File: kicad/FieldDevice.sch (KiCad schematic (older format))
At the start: 13 parts

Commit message: Adding more features to the design
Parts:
- removed RV?: POT, symbol POT
- added J? (x4): JUMPER_1x2, symbol JUMPER_1x2
- added R? (x4): NPOP, symbol R
- added SW? (x2): SW_PUSH, symbol SW_PUSH
- added U?: MCP4017T-502E, symbol MCP4017T-502E
- R?: value 0 -> 0Ω
- R?: value 10k -> 9k1Ω
- R?: value 5k -> 4k7Ω
- TH?: value THERMISTOR -> PTC
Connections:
- net labels added: Display, OverTemp, Set
- wire segments 44 -> 73
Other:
- note added: "# Seperate ADC for isolation away from the Micro. \n Would this be advixable/necessary?\n# Would the PTC really provide any form of protection?\n# Could a Digital Potentiometer be used here?\n# How would this really be calibrated?\n"
- note added: "Hard wired I²C \naddress '0101111'"
- note added: "I²C Address '1010000'"
- note added: "The minimal configuration for the XBEE is \nVcc, GND, DIN and DOUT"
- moved on the sheet: D?, H?, R?, TH?

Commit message: Completed schematic, layout and gerbers. 2L_1
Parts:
- removed D?: D, symbol D
- removed J? (x4): JUMPER_1x2, symbol JUMPER_1x2
- removed R?: 9k1Ω, symbol R
- removed R?: 4k7Ω, symbol R
- removed R? (x4): NPOP, symbol R
- removed SW? (x2): SW_PUSH, symbol SW_PUSH
- removed TH?: PTC, symbol THERMISTOR
- removed U?: MCP4017T-502E, symbol MCP4017T-502E
- added R102, R107, R108: 0Ω, Resistors_SMD:R_0805, symbol R
- added R103, R110: 4k7Ω, Resistors_SMD:R_0805, symbol R
- H101: renamed from H?; footprint (none) -> CE_Header:CE_Header
- H102: renamed from H?; footprint (none) -> FieldDevice_Footprints:XBEE_S2C
- R101, R104, R105, R106, R109: renamed from R?; footprint (none) -> Resistors_SMD:R_0805
- U101: renamed from U?; footprint (none) -> Housings_SOIC:SOIC-8_3.9x4.9mm_Pitch1.27mm
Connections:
- net labels added: ANLG_1, CLK, CS, MOSI, REG_SEL
- net labels removed: Set, TEST_NEG, TEST_POS, VMesure
- wire segments 73 -> 56
- no-connect marks 14 -> 17
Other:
- note removed: "Fixed address of 0x90"
- note removed: "Hard wired I²C \naddress '0101111'"
- note removed: "Voltage Sensor"

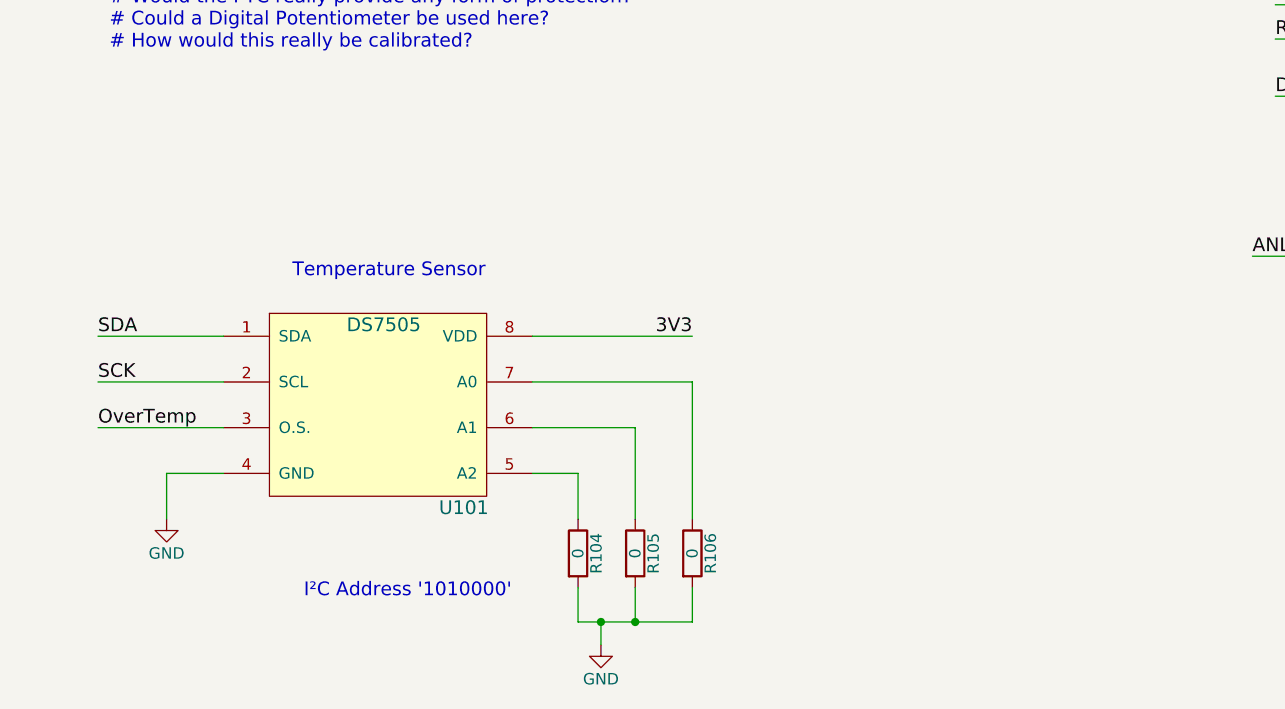
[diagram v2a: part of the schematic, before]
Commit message: added the missing pullup resistors 2L_2
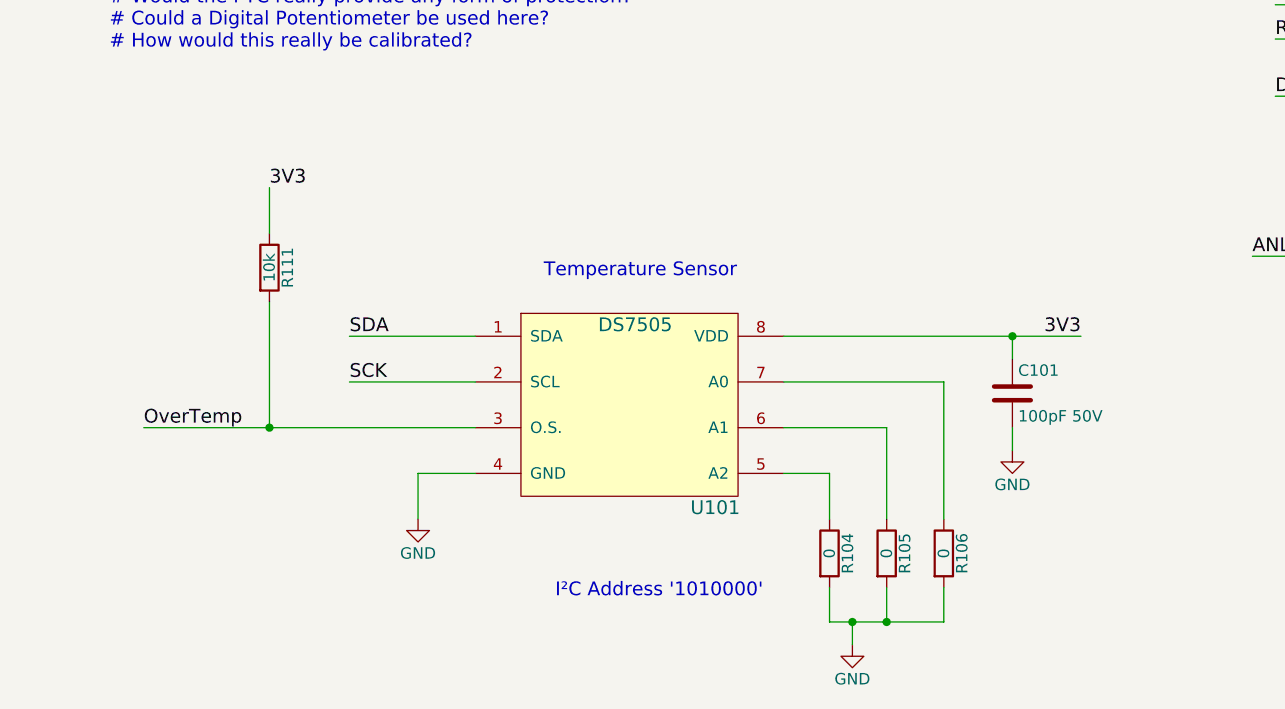
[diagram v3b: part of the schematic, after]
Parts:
- added C101: 100pF 50V, Capacitors_SMD:C_0805, symbol C
- added R111: 10k, Resistors_SMD:R_0805, symbol R
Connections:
- net 3V3: now also C101.1, R111.1
- net GND: now also C101.2
- net OverTemp: now also R111.2
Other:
- moved on the sheet: R104, R105, R106, U101
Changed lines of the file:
@@
 L DS7505 U101
 U 1 1 59347421
-P 2250 6100
-F 0 "U101" H 2600 5650 60  0000 C CNN
-F 1 "DS7505" H 2250 6450 60  0000 C CNN
-F 2 "Housings_SOIC:SOIC-8_3.9x4.9mm_Pitch1.27mm" H 2250 5900 60  0001 C CNN
-F 3 "" H 2250 5900 60  0000 C CNN
-	1    2250 6100
-	1    0    0    -1
-$EndComp
-Text Label 3600 5800 2    60   ~ 0
+P 3350 6100
+F 0 "U101" H 3700 5650 60  0000 C CNN
+F 1 "DS7505" H 3350 6450 60  0000 C CNN
+F 2 "Housings_SOIC:SOIC-8_3.9x4.9mm_Pitch1.27mm" H 3350 5900 60  0001 C CNN
+F 3 "" H 3350 5900 60  0000 C CNN
+	1    3350 6100
+	1    0    0    -1
+$EndComp
+Text Label 5300 5800 2    60   ~ 0
 3V3
 $Comp
 L GND #PWR04
 U 1 1 59347521
-P 1300 6600
-F 0 "#PWR04" H 1300 6350 50  0001 C CNN
-F 1 "GND" H 1300 6450 50  0000 C CNN
-F 2 "" H 1300 6600 50  0000 C CNN
-F 3 "" H 1300 6600 50  0000 C CNN
-	1    1300 6600
+P 2400 6600
+F 0 "#PWR04" H 2400 6350 50  0001 C CNN
+F 1 "GND" H 2400 6450 50  0000 C CNN
+F 2 "" H 2400 6600 50  0000 C CNN
+F 3 "" H 2400 6600 50  0000 C CNN
+	1    2400 6600
 	1    0    0    -1
 $EndComp
@@
 L R R104
 U 1 1 593475EC
-P 3100 6750
-F 0 "R104" V 3180 6750 50  0000 C CNN
-F 1 "0" V 3100 6750 50  0000 C CNN
-F 2 "Resistors_SMD:R_0805" V 3030 6750 50  0001 C CNN
-F 3 "" H 3100 6750 50  0000 C CNN
-	1    3100 6750
+P 4200 6750
+F 0 "R104" V 4280 6750 50  0000 C CNN
+F 1 "0" V 4200 6750 50  0000 C CNN
+F 2 "Resistors_SMD:R_0805" V 4130 6750 50  0001 C CNN
+F 3 "" H 4200 6750 50  0000 C CNN
+	1    4200 6750
 	1    0    0    -1
 $EndComp
@@
 L R R105
 U 1 1 59347631
-P 3350 6750
-F 0 "R105" V 3430 6750 50  0000 C CNN
-F 1 "0" V 3350 6750 50  0000 C CNN
-F 2 "Resistors_SMD:R_0805" V 3280 6750 50  0001 C CNN
-F 3 "" H 3350 6750 50  0000 C CNN
-	1    3350 6750
+P 4450 6750
+F 0 "R105" V 4530 6750 50  0000 C CNN
+F 1 "0" V 4450 6750 50  0000 C CNN
+F 2 "Resistors_SMD:R_0805" V 4380 6750 50  0001 C CNN
+F 3 "" H 4450 6750 50  0000 C CNN
+	1    4450 6750
 	1    0    0    -1
 $EndComp
@@
 L R R106
 U 1 1 5934765B
-P 3600 6750
-F 0 "R106" V 3680 6750 50  0000 C CNN
-F 1 "0" V 3600 6750 50  0000 C CNN
-F 2 "Resistors_SMD:R_0805" V 3530 6750 50  0001 C CNN
-F 3 "" H 3600 6750 50  0000 C CNN
-	1    3600 6750
+P 4700 6750
+F 0 "R106" V 4780 6750 50  0000 C CNN
+F 1 "0" V 4700 6750 50  0000 C CNN
+F 2 "Resistors_SMD:R_0805" V 4630 6750 50  0001 C CNN
+F 3 "" H 4700 6750 50  0000 C CNN
+	1    4700 6750
 	1    0    0    -1
 $EndComp
@@
 L GND #PWR05
 U 1 1 59347764
-P 3200 7150
-F 0 "#PWR05" H 3200 6900 50  0001 C CNN
-F 1 "GND" H 3200 7000 50  0000 C CNN
-F 2 "" H 3200 7150 50  0000 C CNN
-F 3 "" H 3200 7150 50  0000 C CNN
-	1    3200 7150
+P 4300 7150
+F 0 "#PWR05" H 4300 6900 50  0001 C CNN
+F 1 "GND" H 4300 7000 50  0000 C CNN
+F 2 "" H 4300 7150 50  0000 C CNN
+F 3 "" H 4300 7150 50  0000 C CNN
+	1    4300 7150
 	1    0    0    -1
 $EndComp
@@
 Text Label 4900 2300 2    60   ~ 0
 SDA
-Text Label 1000 5800 0    60   ~ 0
+Text Label 2100 5800 0    60   ~ 0
 SDA
-Text Label 1000 6000 0    60   ~ 0
+Text Label 2100 6000 0    60   ~ 0
 SCK
-Text Notes 1850 5550 0    60   ~ 0
+Text Notes 2950 5550 0    60   ~ 0
 Temperature Sensor
 Text Notes 1050 4550 0    60   ~ 0
 # Seperate ADC for isolation away from the Micro. \n    Would this be advixable/necessary?\n# Would the PTC really provide any form of protection?\n# Could a Digital Potentiometer be used here?\n# How would this really be calibrated?\n
-Text Notes 1900 6950 0    60   ~ 0
+Text Notes 3000 6950 0    60   ~ 0
 I²C Address '1010000'
 Text Notes 7500 1200 0    60   ~ 0
 The minimal configuration for the XBEE is \nVcc, GND, DIN and DOUT
-Text Label 1000 6200 0    60   ~ 0
+Text Label 1200 6200 0    60   ~ 0
 OverTemp
 $Sheet
@@
 	6100 2100 5650 2100
 Wire Wire Line
-	2900 5800 3600 5800
-Wire Wire Line
-	1550 6400 1300 6400
-Wire Wire Line
-	1300 6400 1300 6600
-Wire Wire Line
-	1550 5800 1000 5800
-Wire Wire Line
-	1550 6000 1000 6000
-Wire Wire Line
-	1550 6200 1000 6200
-Wire Wire Line
-	3100 6900 3100 7050
-Wire Wire Line
-	3100 7050 3600 7050
-Wire Wire Line
-	3600 7050 3600 6900
-Wire Wire Line
-	3350 6900 3350 7050
-Connection ~ 3350 7050
-Wire Wire Line
-	3200 7050 3200 7150
-Connection ~ 3200 7050
-Wire Wire Line
-	2900 6400 3100 6400
-Wire Wire Line
-	3100 6400 3100 6600
-Wire Wire Line
-	2900 6200 3350 6200
-Wire Wire Line
-	3350 6200 3350 6600
-Wire Wire Line
-	2900 6000 3600 6000
-Wire Wire Line
-	3600 6000 3600 6600
+	4000 5800 5300 5800
+Wire Wire Line
+	2650 6400 2400 6400
+Wire Wire Line
+	2400 6400 2400 6600
+Wire Wire Line
+	2650 5800 2100 5800
+Wire Wire Line
+	2650 6000 2100 6000
+Wire Wire Line
+	1200 6200 2650 6200
+Wire Wire Line
+	4200 6900 4200 7050
+Wire Wire Line
+	4200 7050 4700 7050
+Wire Wire Line
+	4700 7050 4700 6900
+Wire Wire Line
+	4450 6900 4450 7050
+Connection ~ 4450 7050
+Wire Wire Line
+	4300 7050 4300 7150
+Connection ~ 4300 7050
+Wire Wire Line
+	4000 6400 4200 6400
+Wire Wire Line
+	4200 6400 4200 6600
+Wire Wire Line
+	4000 6200 4450 6200
+Wire Wire Line
+	4450 6200 4450 6600
+Wire Wire Line
+	4000 6000 4700 6000
+Wire Wire Line
+	4700 6000 4700 6600
 Wire Wire Line
 	3550 2300 4900 2300
@@
 3V3
 NoConn ~ 1550 1100
+$Comp
+L R R111
+U 1 1 595BD879
+P 1750 5500
+F 0 "R111" V 1830 5500 50  0000 C CNN
+F 1 "10k" V 1750 5500 50  0000 C CNN
+F 2 "Resistors_SMD:R_0805" V 1680 5500 50  0001 C CNN
+F 3 "" H 1750 5500 50  0000 C CNN
+	1    1750 5500
+	1    0    0    -1
+$EndComp
+Wire Wire Line
+	1750 5650 1750 6200
+Connection ~ 1750 6200
+Wire Wire Line
+	1750 5350 1750 5150
+Text Label 1750 5150 0    60   ~ 0
+3V3
+Wire Wire Line
+	5000 5800 5000 5900
+$Comp
+L C C101
+U 1 1 595BE884
+P 5000 6050
+F 0 "C101" H 5025 6150 50  0000 L CNN
+F 1 "100pF 50V" H 5025 5950 50  0000 L CNN
+F 2 "Capacitors_SMD:C_0805" H 5038 5900 30  0001 C CNN
+F 3 "" H 5000 6050 60  0000 C CNN
+F 4 "Value" H 5000 6050 60  0001 C CNN "Link"
+	1    5000 6050
+	1    0    0    -1
+$EndComp
+$Comp
+L GND #PWR06
+U 1 1 595BE9B4
+P 5000 6300
+F 0 "#PWR06" H 5000 6050 50  0001 C CNN
+F 1 "GND" H 5000 6150 50  0000 C CNN
+F 2 "" H 5000 6300 50  0000 C CNN
+F 3 "" H 5000 6300 50  0000 C CNN
+	1    5000 6300
+	1    0    0    -1
+$EndComp
+Wire Wire Line
+	5000 6200 5000 6300
+Connection ~ 5000 5800
 $EndSCHEMATC

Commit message: Change over to use the DOGM081 adapter board rather than direct connect - also used the CE_Socket!
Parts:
- H101: footprint CE_Header:CE_Header -> CE_Header:CE_Socket
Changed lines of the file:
@@
 F 0 "H101" H 3250 700 60  0000 C CNN
 F 1 "CE_Header" H 2550 3000 60  0000 C CNN
-F 2 "CE_Header:CE_Header" H 2150 2300 60  0001 C CNN
+F 2 "CE_Header:CE_Socket" H 2150 2300 60  0001 C CNN
 F 3 "" H 2150 2300 60  0000 C CNN
 	1    2550 1900

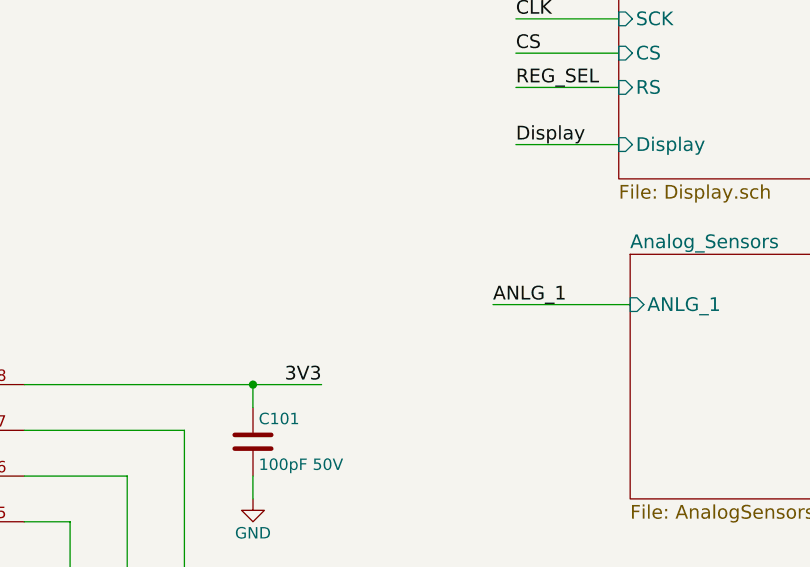
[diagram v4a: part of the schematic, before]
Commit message: Testing the idea of a zenner on the V Input. Added test code for the voltage test
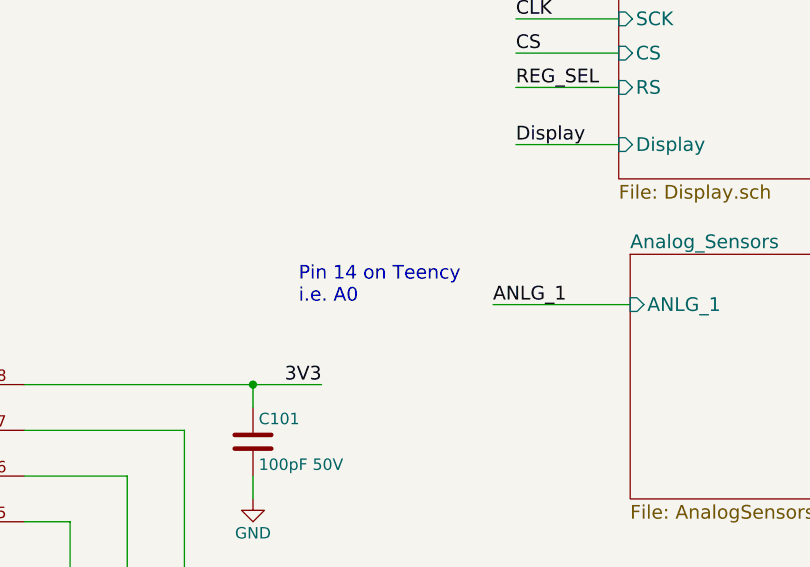
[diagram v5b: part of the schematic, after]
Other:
- note added: "Pin 14 on Teency\ni.e. A0"
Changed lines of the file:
@@
 	5000 6200 5000 6300
 Connection ~ 5000 5800
+Text Notes 5200 5450 0    60   ~ 0
+Pin 14 on Teency\ni.e. A0
 $EndSCHEMATC

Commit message: Enhanced display port connector and layout - Submit to OSH Park
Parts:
- added D101, D102: LED, Diodes_SMD:D_0805, symbol LED
- added R112, R113: 680Ω, Resistors_SMD:R_0805_HandSoldering, symbol R
- C101: footprint Capacitors_SMD:C_0805 -> Capacitors_SMD:C_0805_HandSoldering
- H101: value CE_Header -> CE_Socket; Link (none) -> Value
- R101, R102, R103, R104, R105, R106, R107, R108, R109, R110, R111: footprint Resistors_SMD:R_0805 -> Resistors_SMD:R_0805_HandSoldering
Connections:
- net GND: now also R112.1, R113.1
- net RX: now also D102.2 (A)
- net TX: now also D101.2 (A)
- net CLK renamed SPI_CLK
- net SCK renamed I2C_SCK
- new net: D101.1 (K), R112.2
- new net: D102.1 (K), R113.2
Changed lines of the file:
@@
 P 2550 1900
 F 0 "H101" H 3250 700 60  0000 C CNN
-F 1 "CE_Header" H 2550 3000 60  0000 C CNN
+F 1 "CE_Socket" H 2550 3000 60  0000 C CNN
 F 2 "CE_Header:CE_Socket" H 2150 2300 60  0001 C CNN
 F 3 "" H 2150 2300 60  0000 C CNN
+F 4 "Value" H 2550 1900 60  0001 C CNN "Link"
 	1    2550 1900
 	1    0    0    -1
@@
 F 0 "R109" V 3980 1700 50  0000 C CNN
 F 1 "0" V 3900 1700 50  0000 C CNN
-F 2 "Resistors_SMD:R_0805" V 3830 1700 50  0001 C CNN
+F 2 "Resistors_SMD:R_0805_HandSoldering" V 3830 1700 50  0001 C CNN
 F 3 "" H 3900 1700 50  0000 C CNN
 	1    3900 1700
@@
 F 0 "R101" V 1230 1700 50  0000 C CNN
 F 1 "0Ω" V 1150 1700 50  0000 C CNN
-F 2 "Resistors_SMD:R_0805" V 1080 1700 50  0001 C CNN
+F 2 "Resistors_SMD:R_0805_HandSoldering" V 1080 1700 50  0001 C CNN
 F 3 "" H 1150 1700 50  0000 C CNN
 	1    1150 1700
 	0    1    1    0
 $EndComp
-Text Label 5650 2000 0    60   ~ 0
+Text Label 5300 2000 0    60   ~ 0
 TX
-Text Label 5650 2100 0    60   ~ 0
+Text Label 5300 2100 0    60   ~ 0
 RX
 NoConn ~ 6100 2200
@@
 F 0 "R104" V 4280 6750 50  0000 C CNN
 F 1 "0" V 4200 6750 50  0000 C CNN
-F 2 "Resistors_SMD:R_0805" V 4130 6750 50  0001 C CNN
+F 2 "Resistors_SMD:R_0805_HandSoldering" V 4130 6750 50  0001 C CNN
 F 3 "" H 4200 6750 50  0000 C CNN
 	1    4200 6750
@@
 F 0 "R105" V 4530 6750 50  0000 C CNN
 F 1 "0" V 4450 6750 50  0000 C CNN
-F 2 "Resistors_SMD:R_0805" V 4380 6750 50  0001 C CNN
+F 2 "Resistors_SMD:R_0805_HandSoldering" V 4380 6750 50  0001 C CNN
 F 3 "" H 4450 6750 50  0000 C CNN
 	1    4450 6750
@@
 F 0 "R106" V 4780 6750 50  0000 C CNN
 F 1 "0" V 4700 6750 50  0000 C CNN
-F 2 "Resistors_SMD:R_0805" V 4630 6750 50  0001 C CNN
+F 2 "Resistors_SMD:R_0805_HandSoldering" V 4630 6750 50  0001 C CNN
 F 3 "" H 4700 6750 50  0000 C CNN
 	1    4700 6750
@@
 $EndComp
 Text Label 650  2300 0    60   ~ 0
-SCK
+I2C_SCK
 Text Label 4900 2300 2    60   ~ 0
 SDA
@@
 SDA
 Text Label 2100 6000 0    60   ~ 0
-SCK
+I2C_SCK
 Text Notes 2950 5550 0    60   ~ 0
 Temperature Sensor
@@
 	1300 1700 1550 1700
 Wire Wire Line
-	6100 2000 5650 2000
-Wire Wire Line
-	6100 2100 5650 2100
+	5300 2000 6100 2000
+Wire Wire Line
+	5300 2100 6100 2100
 Wire Wire Line
 	4000 5800 5300 5800
@@
 F3 "RS" I L 6600 4500 60
 F4 "MOSI" I L 6600 4050 60
-F5 "SCK" I L 6600 4200 60
+F5 "SPI_SCK" I L 6600 4200 60
 F6 "CS" I L 6600 4350 60
 F7 "Display" I L 6600 4750 60
@@
 CS
 Text Label 6150 4200 0    60   ~ 0
-CLK
+SPI_CLK
 Text Label 6150 4050 0    60   ~ 0
 MOSI
@@
 NoConn ~ 6100 2300
 Text Label 650  1500 0    60   ~ 0
-CLK
+SPI_CLK
 $Comp
 L R R107
@@
 F 0 "R107" V 3930 2500 50  0000 C CNN
 F 1 "0Ω" V 3850 2500 50  0000 C CNN
-F 2 "Resistors_SMD:R_0805" V 3780 2500 50  0001 C CNN
+F 2 "Resistors_SMD:R_0805_HandSoldering" V 3780 2500 50  0001 C CNN
 F 3 "" H 3850 2500 50  0000 C CNN
 	1    3850 2500
@@
 F 0 "R108" V 3930 2700 50  0000 C CNN
 F 1 "0Ω" V 3850 2700 50  0000 C CNN
-F 2 "Resistors_SMD:R_0805" V 3780 2700 50  0001 C CNN
+F 2 "Resistors_SMD:R_0805_HandSoldering" V 3780 2700 50  0001 C CNN
 F 3 "" H 3850 2700 50  0000 C CNN
 	1    3850 2700
@@
 F 0 "R102" V 1380 2700 50  0000 C CNN
 F 1 "0Ω" V 1300 2700 50  0000 C CNN
-F 2 "Resistors_SMD:R_0805" V 1230 2700 50  0001 C CNN
+F 2 "Resistors_SMD:R_0805_HandSoldering" V 1230 2700 50  0001 C CNN
 F 3 "" H 1300 2700 50  0000 C CNN
 	1    1300 2700
@@
 F 0 "R103" V 1430 2100 50  0000 C CNN
 F 1 "4k7Ω" V 1350 2100 50  0000 C CNN
-F 2 "Resistors_SMD:R_0805" V 1280 2100 50  0001 C CNN
+F 2 "Resistors_SMD:R_0805_HandSoldering" V 1280 2100 50  0001 C CNN
 F 3 "" H 1350 2100 50  0000 C CNN
 	1    1350 2100
@@
 F 0 "R110" V 4680 2050 50  0000 C CNN
 F 1 "4k7Ω" V 4600 2050 50  0000 C CNN
-F 2 "Resistors_SMD:R_0805" V 4530 2050 50  0001 C CNN
+F 2 "Resistors_SMD:R_0805_HandSoldering" V 4530 2050 50  0001 C CNN
 F 3 "" H 4600 2050 50  0000 C CNN
 	1    4600 2050
@@
 F 0 "R111" V 1830 5500 50  0000 C CNN
 F 1 "10k" V 1750 5500 50  0000 C CNN
-F 2 "Resistors_SMD:R_0805" V 1680 5500 50  0001 C CNN
+F 2 "Resistors_SMD:R_0805_HandSoldering" V 1680 5500 50  0001 C CNN
 F 3 "" H 1750 5500 50  0000 C CNN
 	1    1750 5500
@@
 F 0 "C101" H 5025 6150 50  0000 L CNN
 F 1 "100pF 50V" H 5025 5950 50  0000 L CNN
-F 2 "Capacitors_SMD:C_0805" H 5038 5900 30  0001 C CNN
+F 2 "Capacitors_SMD:C_0805_HandSoldering" H 5038 5900 30  0001 C CNN
 F 3 "" H 5000 6050 60  0000 C CNN
 F 4 "Value" H 5000 6050 60  0001 C CNN "Link"
@@
 Text Notes 5200 5450 0    60   ~ 0
 Pin 14 on Teency\ni.e. A0
+$Comp
+L LED D101
+U 1 1 59CB7CCC
+P 5500 2650
+F 0 "D101" H 5500 2750 50  0000 C CNN
+F 1 "LED" H 5500 2550 50  0000 C CNN
+F 2 "Diodes_SMD:D_0805" H 5500 2650 60  0001 C CNN
+F 3 "" H 5500 2650 60  0000 C CNN
+	1    5500 2650
+	0    -1   -1   0
+$EndComp
+$Comp
+L LED D102
+U 1 1 59CB7D69
+P 5800 2650
+F 0 "D102" H 5800 2750 50  0000 C CNN
+F 1 "LED" H 5800 2550 50  0000 C CNN
+F 2 "Diodes_SMD:D_0805" H 5800 2650 60  0001 C CNN
+F 3 "" H 5800 2650 60  0000 C CNN
+	1    5800 2650
+	0    -1   -1   0
+$EndComp
+Wire Wire Line
+	5500 2450 5500 2000
+Connection ~ 5500 2000
+Wire Wire Line
+	5800 2450 5800 2100
+Connection ~ 5800 2100
+Wire Wire Line
+	5500 3500 5800 3500
+$Comp
+L GND #PWR07
+U 1 1 59CB7FF0
+P 5650 3750
+F 0 "#PWR07" H 5650 3500 50  0001 C CNN
+F 1 "GND" H 5650 3600 50  0000 C CNN
+F 2 "" H 5650 3750 50  0000 C CNN
+F 3 "" H 5650 3750 50  0000 C CNN
+	1    5650 3750
+	1    0    0    -1
+$EndComp
+Wire Wire Line
+	5650 3750 5650 3500
+Connection ~ 5650 3500
+$Comp
+L R R112
+U 1 1 59CB849B
+P 5500 3150
+F 0 "R112" V 5580 3150 50  0000 C CNN
+F 1 "680Ω" V 5500 3150 50  0000 C CNN
+F 2 "Resistors_SMD:R_0805_HandSoldering" V 5430 3150 50  0001 C CNN
+F 3 "" H 5500 3150 50  0000 C CNN
+	1    5500 3150
+	-1   0    0    1
+$EndComp
+$Comp
+L R R113
+U 1 1 59CB8725
+P 5800 3150
+F 0 "R113" V 5880 3150 50  0000 C CNN
+F 1 "680Ω" V 5800 3150 50  0000 C CNN
+F 2 "Resistors_SMD:R_0805_HandSoldering" V 5730 3150 50  0001 C CNN
+F 3 "" H 5800 3150 50  0000 C CNN
+	1    5800 3150
+	-1   0    0    1
+$EndComp
+Wire Wire Line
+	5500 2850 5500 3000
+Wire Wire Line
+	5500 3300 5500 3500
+Wire Wire Line
+	5800 3500 5800 3300
+Wire Wire Line
+	5800 3000 5800 2850
 $EndSCHEMATC
